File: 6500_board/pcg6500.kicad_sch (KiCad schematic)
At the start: 42 parts, among them CN1 CharROM ADAPTER, CN2 USERPORT, IC1 74LS123, IC10 74LS157, IC11 74LS157, IC12 D2101AL-4, IC13 D2101AL-4, IC14 D2101AL-4, IC15 D2101AL-4, IC2 74LS42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

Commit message: housekeeping
added missing Cap values
improvements in signal naming and schematic layout
no functional changes
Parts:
- C20, C21, C22, C23, C24, C25, C26: value 100nF -> 10nF
- C4: value C_Polarized -> 100uF
- C8: now not fitted; now left out of the parts list
- R1: value 10 -> 10R
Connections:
- net ~{WRITE_{RAM}}_{_delayed} renamed ~{WRITE_{RAM}}_{_delay}
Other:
- note added: "2.24 µs high pulse"
- note added: "2.24 µs low pulse"
- note added: "VR1, C1 and C4 values taken from standard implementations; unreadable in original images"
- note added: "t_{w} = K*R_{t}*C_{EXT}*(1+(0.7/R_{T})) K= 0.28 (for LS123) R_{T} in KOhm C_{EXT} in pF t_{W} in ns"
- note removed: "DATA 0-3"
- moved on the sheet: CN2, IC15, IC8A, J2

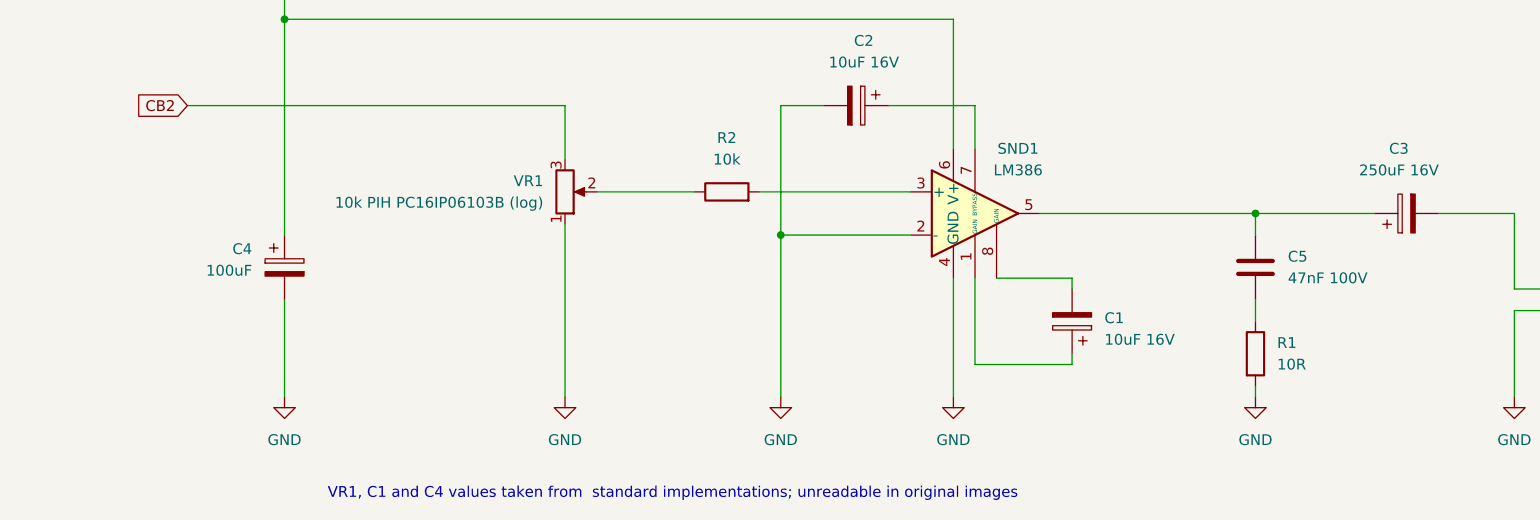
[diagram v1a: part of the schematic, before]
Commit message: BOM adjustment
- changed excessive voltage rating of  audio related capacitors to more realistic values
- added cn2 connector to bom
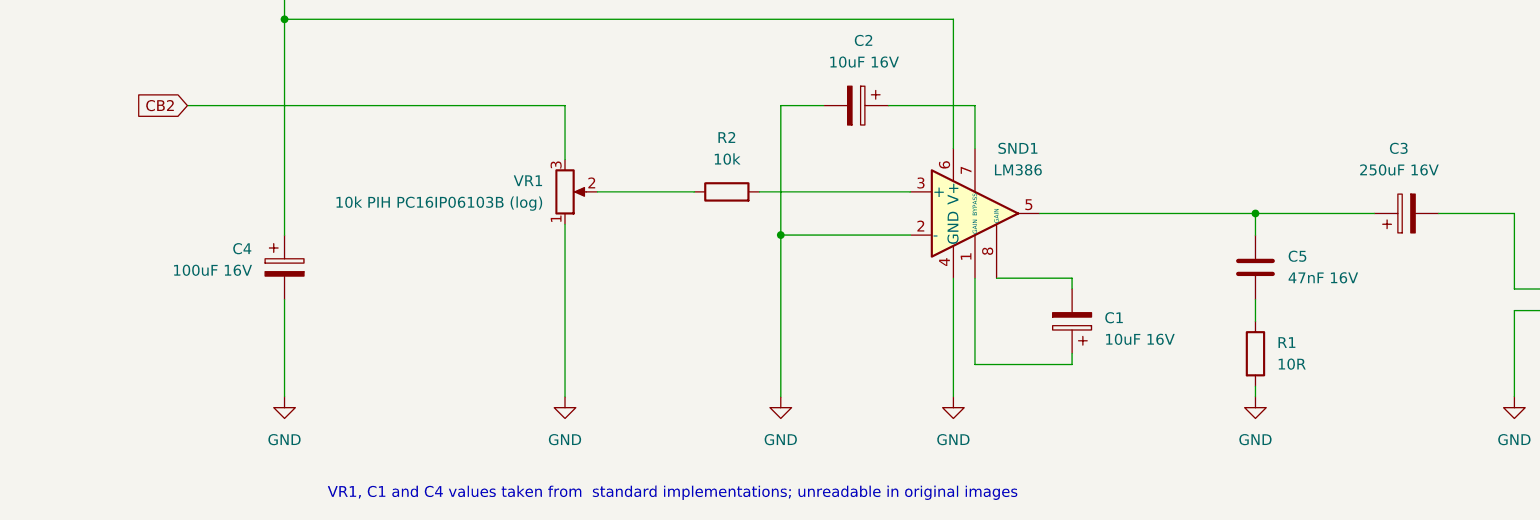
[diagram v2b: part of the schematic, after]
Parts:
- C4: value 100uF -> 100uF 16V
- C5: value 47nF 100V -> 47nF 16V
- CN2: now in the parts list
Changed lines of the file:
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@@
 			)
 		)
-		(property "Value" "100uF"
+		(property "Value" "100uF 16V"
 			(at 240.03 372.4909 0)
 			(effects
@@
 		(unit 1)
 		(exclude_from_sim no)
-		(in_bom no)
+		(in_bom yes)
 		(on_board yes)
 		(dnp no)
@@
 		(fields_autoplaced yes)
 		(property "Reference" "C5"
-			(at 361.95 370.84 0)
+			(at 361.95 370.8399 0)
 			(effects
 				(font
@@
 			)
 		)
-		(property "Value" "47nF 100V"
-			(at 361.95 373.38 0)
+		(property "Value" "47nF 16V"
+			(at 361.95 373.3799 0)
 			(effects
 				(font
